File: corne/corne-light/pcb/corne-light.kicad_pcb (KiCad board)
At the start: 2 copper layers, 274.7 x 91.4 mm, 112 parts, among them J1 MJ-4PP-9, J2 OLED, J6 MJ-4PP-9, J7 OLED, SW1 SW_PUSH, SW10 SW_PUSH, SW11 SW_PUSH, SW12 SW_PUSH, SW13 SW_PUSH, SW14 SW_PUSH, SW15 SW_PUSH, SW16 SW_PUSH, SW17 SW_PUSH, SW18 SW_PUSH, SW19 SW_PUSH, SW2 SW_PUSH, SW20 SW_PUSH, SW21 SW_PUSH, SW22 SW_PUSH, SW23 SW_PUSH, SW24 SW_PUSH, SW25 SW_PUSH, SW26 SW_PUSH, SW27 SW_PUSH, SW28 SW_PUSH, SW29 SW_PUSH, SW3 SW_PUSH, SW30 SW_PUSH, SW31 SW_PUSH, SW32 SW_PUSH, SW33 SW_PUSH, SW34 SW_PUSH, SW35 SW_PUSH, SW36 SW_PUSH, SW37 SW_PUSH, SW38 SW_PUSH, SW39 SW_PUSH, SW4 SW_PUSH, SW40 SW_PUSH, SW41 SW_PUSH, SW42 SW_PUSH, SW5 SW_PUSH, SW6 SW_PUSH, SW7 SW_PUSH, SW8 SW_PUSH, SW9 SW_PUSH, U1 ProMicro, U2 ProMicro

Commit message: corne light: bump version
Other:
- board text added: "cd021db"
- board text removed: "v"

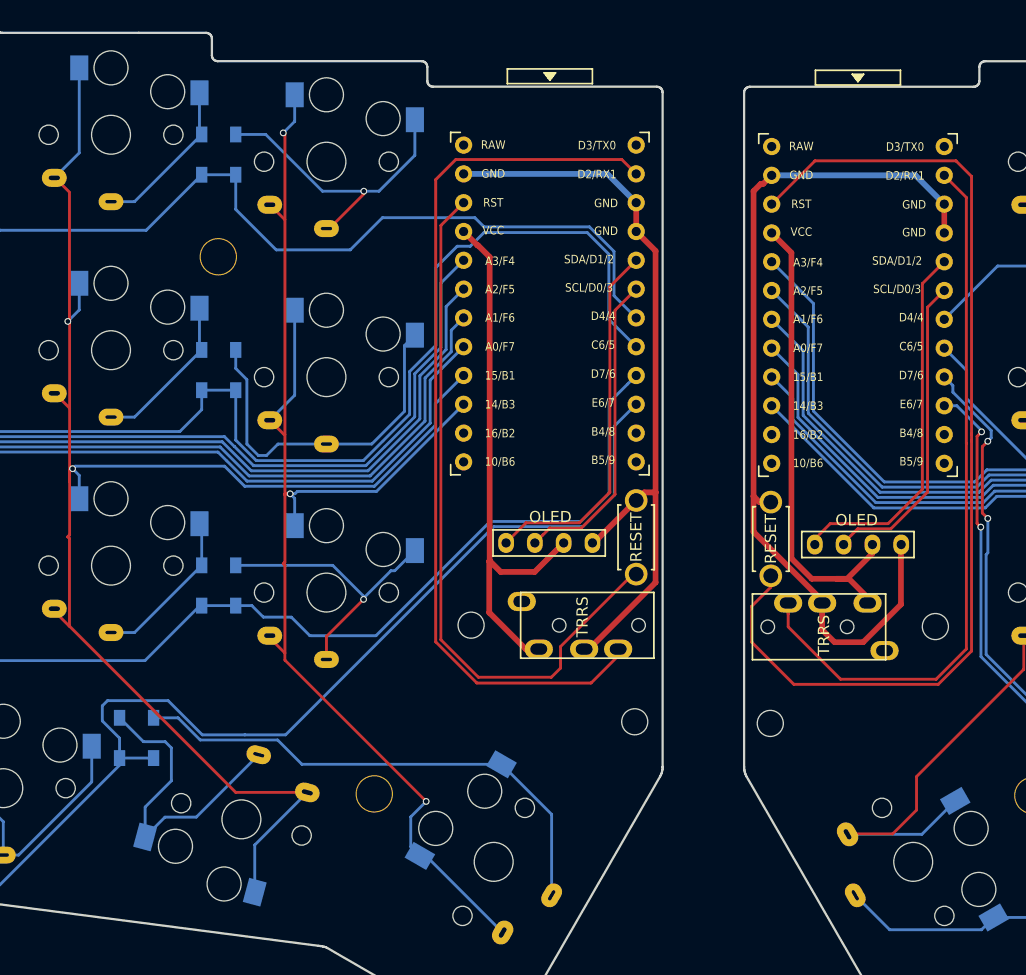
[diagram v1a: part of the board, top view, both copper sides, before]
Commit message: corne-light: rotate SW41 so it's aligned the same as the rest
clean up controller silkscreen
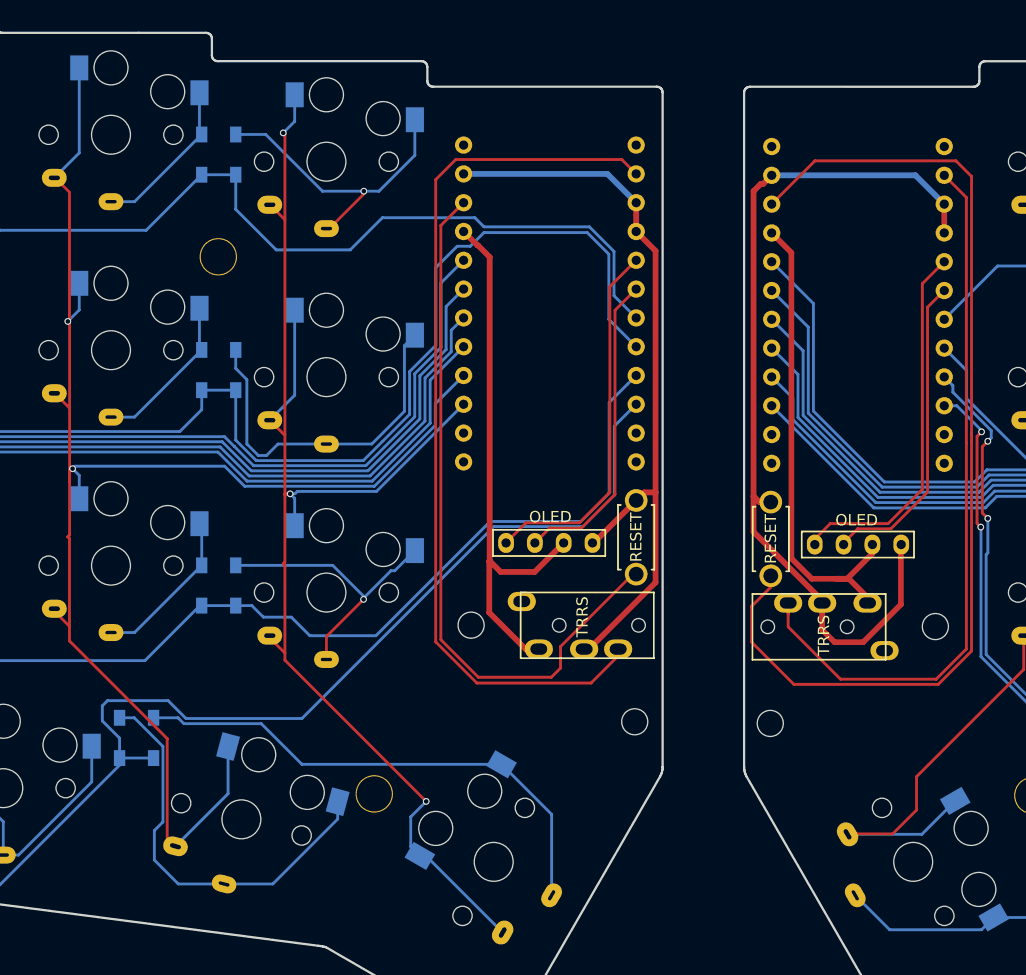
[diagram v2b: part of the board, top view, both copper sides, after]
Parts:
- turned SW20 to -15 degrees
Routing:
- net Net-(D20-Pad2): track 27.5 -> 36.1 mm
- net col4: track 141.6 -> 137.9 mm
- net row3: track 99.2 -> 98.0 mm

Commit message: corne-light: bump version
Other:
- board text added: "d1e75e5"
- board text removed: "cd021db"
